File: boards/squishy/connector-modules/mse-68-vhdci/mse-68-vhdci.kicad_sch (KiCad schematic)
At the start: 14 parts, among them J1 SCSI PHY Mezz, J3 Conn_01x04, J4 VHDCI, U1 M24C02-RMC

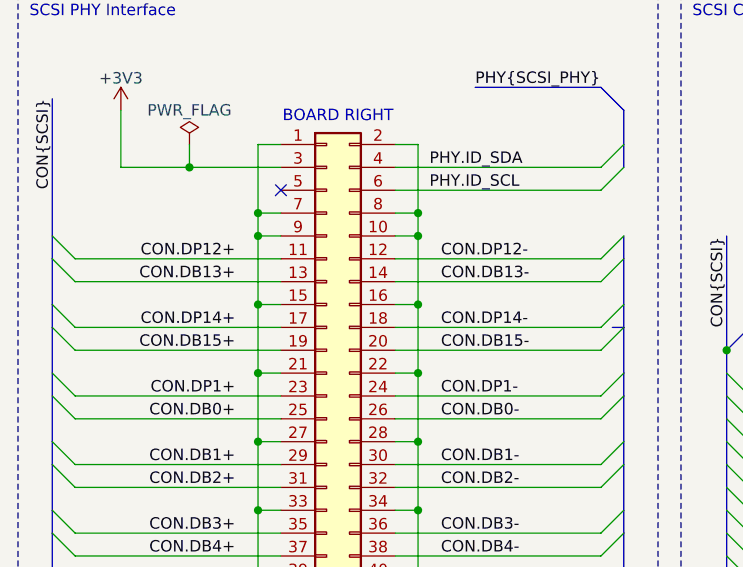
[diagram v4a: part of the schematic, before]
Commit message: squishy: connectors: s/DP12/DB12/g s/DP14/DB14/g
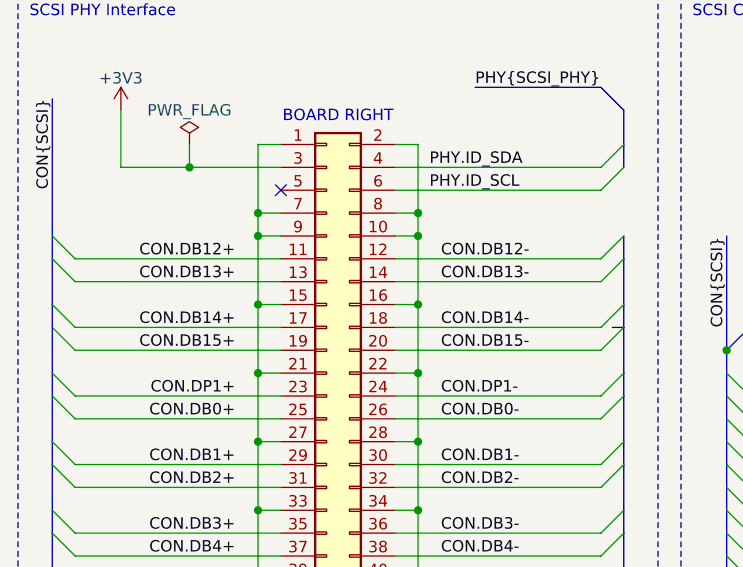
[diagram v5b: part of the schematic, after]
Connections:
- net CON.DP12+ is gone; now on net CON.DB12+: J1.11 (Pin_11)
- net CON.DP12- is gone; now on net CON.DB12-: J1.12 (Pin_12)
- net CON.DP14+ is gone; now on net CON.DB14+: J1.17 (Pin_17)
- net CON.DP14- is gone; now on net CON.DB14-: J1.18 (Pin_18)
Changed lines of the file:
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@@
 		)
 	)
-	(label "CON.DP14-"
+	(label "CON.DB14-"
 		(at 60.96 52.07 0)
 		(fields_autoplaced yes)
@@
 		)
 	)
-	(label "CON.DP12+"
+	(label "CON.DB12+"
 		(at 38.1 44.45 180)
 		(fields_autoplaced yes)
@@
 		)
 	)
-	(label "CON.DP12-"
+	(label "CON.DB12-"
 		(at 60.96 44.45 0)
 		(fields_autoplaced yes)
@@
 		)
 	)
-	(label "CON.DP14+"
+	(label "CON.DB14+"
 		(at 38.1 52.07 180)
 		(fields_autoplaced yes)

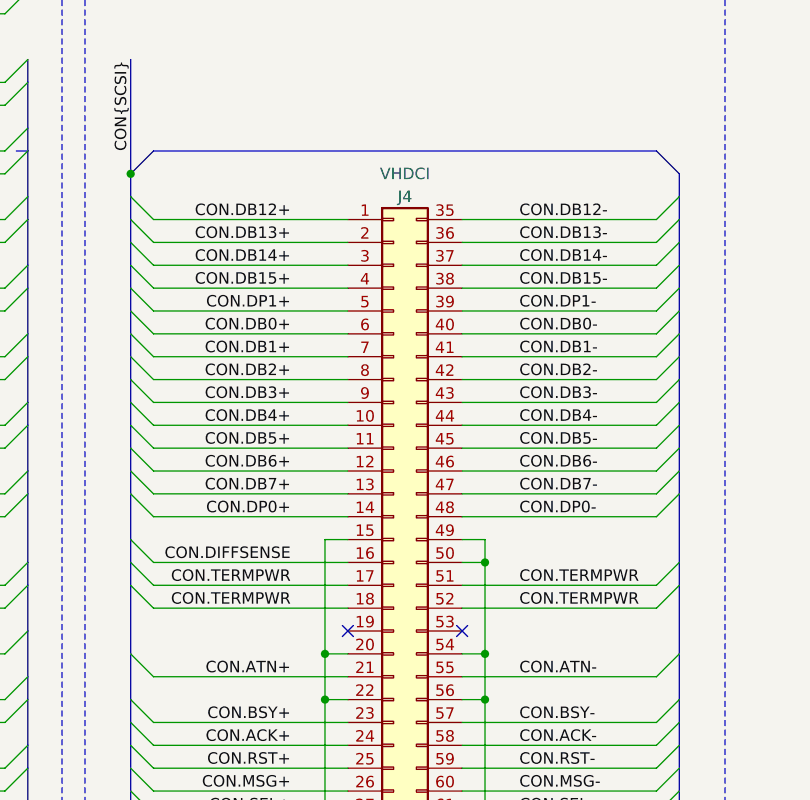
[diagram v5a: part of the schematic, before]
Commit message: squishy: connectors: updated SCSI connector metadata for mse-68-vhdci
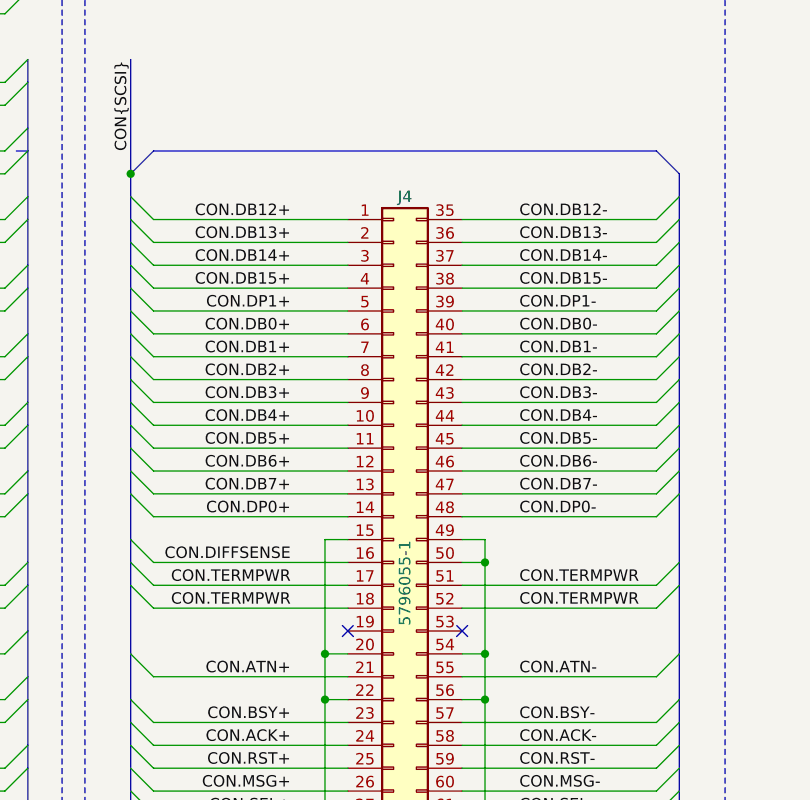
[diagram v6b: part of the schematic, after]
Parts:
- J4: value VHDCI -> 5796055-1; MFR (none) -> TE Connectivity; MPN (none) -> 5796055-1; URL (none) -> https://www.te.com/en/product-5796055-1.html
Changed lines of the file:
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@@
 			)
 		)
-		(property "Value" "VHDCI"
-			(at 123.19 54.61 0)
+		(property "Value" "5796055-1"
+			(at 123.19 100.076 90)
 			(effects
 				(font
@@
 			)
 		)
-		(property "Datasheet" "~"
+		(property "Datasheet" "https://www.te.com/commerce/DocumentDelivery/DDEController?Action=showdoc&DocId=Specification+Or+Standard%7F114-6057%7FD%7Fpdf%7FEnglish%7FENG_SS_114-6057_D.pdf%7F5796055-1"
 			(at 121.92 107.95 0)
 			(effects
@@
 			)
 		)
-		(property "Description" "Generic connector, double row, 02x34 counter clockwise pin numbering scheme (similar to DIP package numbering), with shielding"
+		(property "Description" "CHAMP 0.8mm Right Angle 68-pin VHDCI Connector"
 			(at 123.19 100.076 0)
 			(effects
 				(font
+					(size 1.27 1.27)
+				)
+				(hide yes)
+			)
+		)
+		(property "MFR" "TE Connectivity"
+			(at 123.19 100.33 0)
+			(effects
+				(font
+					(size 1.27 1.27)
+				)
+				(hide yes)
+			)
+		)
+		(property "MPN" "5796055-1"
+			(at 123.19 100.33 0)
+			(effects
+				(font
+					(size 1.27 1.27)
+				)
+				(hide yes)
+			)
+		)
+		(property "URL" "https://www.te.com/en/product-5796055-1.html"
+			(at 123.19 100.33 0)
+			(effects
+				(font

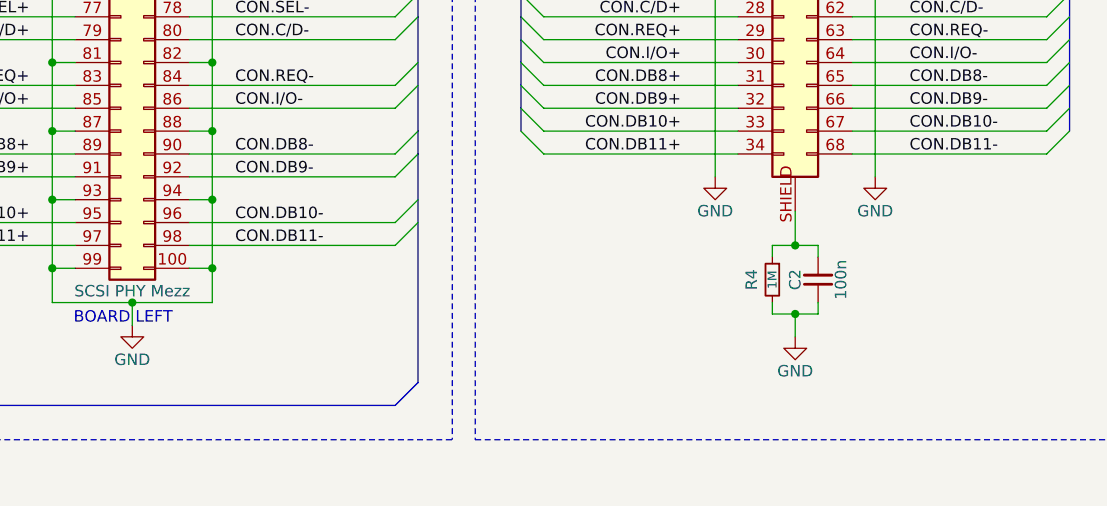
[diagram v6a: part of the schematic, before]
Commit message: squishy: connectors: Length matched, and done ERC and DRC adjustments for cleanliness for the mse-68-vhdci connector interface board
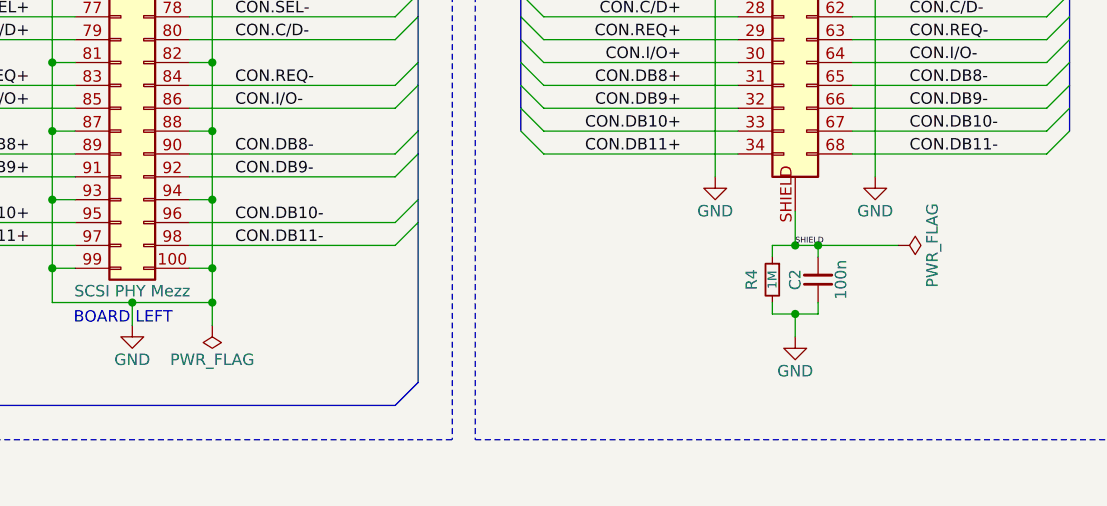
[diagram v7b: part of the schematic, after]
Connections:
- net SHIELD: now reaches C2.2, J4.SHIELD, R4.1
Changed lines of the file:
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@@
 	)
 	(junction
+		(at 125.73 153.67)
+		(diameter 0)
+		(color 0 0 0 0)
+	)
+	(junction
 		(at 40.64 95.25)
 		(diameter 0)
@@
 	)
 	(junction
+		(at 58.42 160.02)
+		(diameter 0)
+		(color 0 0 0 0)
+	)
+	(junction
 		(at 262.89 135.89)
 		(diameter 0)
@@
 	(wire
 		(pts
+			(xy 125.73 153.67) (xy 134.62 153.67)
+		)
+		(stroke
+			(width 0)
+			(type default)
+		)
+	)
+	(wire
+		(pts
 			(xy 78.74 74.93) (xy 55.88 74.93)
 		)
@@
 		)
 	)
+	(wire
+		(pts
+			(xy 58.42 160.02) (xy 58.42 162.56)
+		)
+		(stroke
+			(width 0)
+			(type default)
+		)
+	)
 	(bus
 		(pts
@@
 		)
 	)
+	(label "SHIELD"
+		(at 123.19 153.67 0)
+		(fields_autoplaced yes)
+		(effects
+			(font
+				(size 0.635 0.635)
+			)
+			(justify left bottom)
+		)
+	)
 	(label "CON.DB1+"
 		(at 38.1 67.31 180)
@@
 	)
 	(symbol
+		(lib_id "power:PWR_FLAG")
+		(at 134.62 153.67 270)
+		(unit 1)
+		(exclude_from_sim no)
+		(in_bom yes)
+		(on_board yes)
+		(dnp no)
+		(property "Reference" "#FLG03"
+			(at 136.525 153.67 0)
+			(effects
+				(font
+					(size 1.27 1.27)
+				)
+				(hide yes)
+			)
+		)
+		(property "Value" "PWR_FLAG"
+			(at 138.43 153.67 0)
+			(effects
+				(font
+					(size 1.27 1.27)
+				)
+			)
+		)
+		(property "Footprint" ""
+			(at 134.62 153.67 0)
+			(effects
+				(font
+					(size 1.27 1.27)
+				)
+				(hide yes)
+			)
+		)
+		(property "Datasheet" "~"
+			(at 134.62 153.67 0)
+			(effects
+				(font
+					(size 1.27 1.27)
+				)
+				(hide yes)
+			)
+		)
+		(property "Description" "Special symbol for telling ERC where power comes from"
+			(at 134.62 153.67 0)
+			(effects
+				(font
+					(size 1.27 1.27)
+				)
+				(hide yes)
+			)
+		)
+		(pin "1"
+		)
+		(instances
+			(project "mse-68-vhdci"
+				(path "/bd9eafec-5355-49e4-b2e3-916daacb0a86"
+					(reference "#FLG03")
+					(unit 1)
+				)
+			)
+		)
+	)
+	(symbol
 		(lib_id "lethalbit-graphics:lesbian flag")
 		(at 270.51 172.72 0)
@@
 					(unit 1)
 				)
+			)
+		)
+	)
+	(symbol
+		(lib_id "power:PWR_FLAG")
+		(at 58.42 162.56 180)
+		(unit 1)
+		(exclude_from_sim no)
+		(in_bom yes)
+		(on_board yes)
+		(dnp no)
+		(property "Reference" "#FLG02"
+			(at 58.42 164.465 0)
+			(effects
+				(font
+					(size 1.27 1.27)
+				)
+				(hide yes)
+			)
+		)
+		(property "Value" "PWR_FLAG"
+			(at 58.42 166.37 0)
+			(effects
+				(font
+					(size 1.27 1.27)
+				)
+			)
+		)
+		(property "Footprint" ""
+			(at 58.42 162.56 0)
+			(effects
+				(font
+					(size 1.27 1.27)
+				)
+				(hide yes)
+			)
+		)
+		(property "Datasheet" "~"
+			(at 58.42 162.56 0)
+			(effects
+				(font
+					(size 1.27 1.27)
+				)
+				(hide yes)
+			)
+		)
+		(property "Description" "Special symbol for telling ERC where power comes from"
+			(at 58.42 162.56 0)
+			(effects
+				(font
+					(size 1.27 1.27)
+				)
+				(hide yes)
+			)
+		)
+		(pin "1"
+		)
+		(instances
+			(project "mse-68-vhdci"
+				(path "/bd9eafec-5355-49e4-b2e3-916daacb0a86"
+					(reference "#FLG02")
+					(unit 1)
+				)

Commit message: squishy: connectors: updated part metadata on mse-68-vhdci prior to CAM generation
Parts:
- J3: now left out of the parts list
- J4: SUPPLIER (none) -> TE Connectivity; SUPPLIER_OC (none) -> 5796055-1; SUPPLIER_URL (none) -> https://www.te.com/en/product-5796055-1.html
- R4: MFR (none) -> Vishay Dale; MPN (none) -> CRCW06031M00FKEA; SUPPLIER_OC (none) -> 541-1.00MHDKR-ND; SUPPLIER_URL (none) -> https://www.digikey.com/short/18qqp0zw; Tolerance (none) -> ±1% 1/10W
- U1: MFR (none) -> STMicroelectronics; MPN (none) -> M24C02-RMC6TG; SUPPLIER (none) -> DigiKey; SUPPLIER_OC (none) -> 497-17822-1-ND; SUPPLIER_URL (none) -> https://www.digikey.com/short/r9drrzr3
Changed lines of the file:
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@@
+			)
+		)
+		(property "SUPPLIER" "TE Connectivity"
+			(at 123.19 100.33 0)
+			(effects
+				(font
+					(size 1.27 1.27)
+				)
+				(hide yes)
+			)
+		)
+		(property "SUPPLIER_OC" "5796055-1"
+			(at 123.19 100.33 0)
+			(effects
+				(font
+					(size 1.27 1.27)
+				)
+				(hide yes)
+			)
+		)
+		(property "SUPPLIER_URL" "https://www.te.com/en/product-5796055-1.html"
+			(at 123.19 100.33 0)
+			(effects
+				(font
+					(size 1.27 1.27)
+				)
+				(hide yes)
 			)
 		)
@@
 		(unit 1)
 		(exclude_from_sim no)
-		(in_bom yes)
+		(in_bom no)
 		(on_board yes)
 		(dnp no)
@@
 			)
 		)
-		(property "Datasheet" ""
+		(property "Datasheet" "https://www.vishay.com/docs/20035/dcrcwe3.pdf"
 			(at 120.65 157.48 0)
 			(effects
@@
 			)
 		)
-		(property "MFR" ""
+		(property "MFR" "Vishay Dale"
 			(at 120.65 157.48 90)
 			(effects
@@
 			)
 		)
-		(property "MPN" ""
+		(property "MPN" "CRCW06031M00FKEA"
 			(at 120.65 157.48 90)
 			(effects
@@
 			)
 		)
-		(property "Tolerance" ""
+		(property "Tolerance" "±1% 1/10W"
 			(at 120.65 157.48 0)
 			(effects
@@
 			)
 		)
-		(property "SUPPLIER_OC" ""
+		(property "SUPPLIER_OC" "541-1.00MHDKR-ND"
 			(at 120.65 157.48 0)
 			(effects
@@
 			)
 		)
-		(property "SUPPLIER_URL" ""
+		(property "SUPPLIER_URL" "https://www.digikey.com/short/18qqp0zw"
 			(at 120.65 157.48 0)
 			(effects
@@
 			(at 238.76 147.32 0)
 			(effects
+				(font
+					(size 1.27 1.27)
+				)
+				(hide yes)
+			)
+		)
+		(property "MFR" "STMicroelectronics"
+			(at 238.76 147.32 0)
+			(effects
+				(font
+					(size 1.27 1.27)
+				)
+				(hide yes)
+			)
+		)
+		(property "MPN" "M24C02-RMC6TG"
+			(at 238.76 147.32 0)
+			(effects
+				(font
+					(size 1.27 1.27)
+				)
+				(hide yes)
+			)
+		)
+		(property "SUPPLIER" "DigiKey"
+			(at 238.76 147.32 0)
+			(effects
+				(font
+					(size 1.27 1.27)
+				)
+				(hide yes)
+			)
+		)
+		(property "SUPPLIER_OC" "497-17822-1-ND"
+			(at 238.76 147.32 0)
+			(effects
+				(font
+					(size 1.27 1.27)
+				)
+				(hide yes)
+			)
+		)
+		(property "SUPPLIER_URL" "https://www.digikey.com/short/r9drrzr3"
+			(at 238.76 147.32 0)
+			(effects
